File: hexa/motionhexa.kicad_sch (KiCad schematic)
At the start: 1 part, among them J2 Conn_01x13_Socket

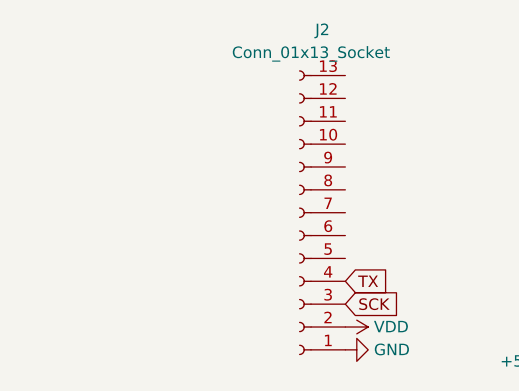
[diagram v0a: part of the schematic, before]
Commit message: checkpoint - hexa design at a size to host two control boards; add board with an rp2040 and a 9dof imu; add a wip for a second board prototype using a BQ25895M to drive higher currents and charge parallel batteries
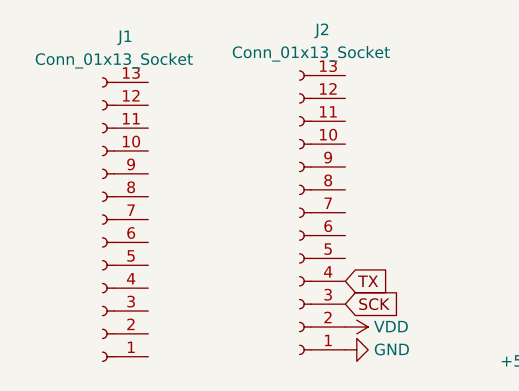
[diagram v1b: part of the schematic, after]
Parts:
- added J1: Conn_01x13_Socket, motionhexa:lipoparallel_pads, symbol Connector:Conn_01x13_Socket
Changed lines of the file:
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@@
+    )
+  )
+  (symbol (lib_id "Connector:Conn_01x13_Socket") (at 89.8652 108.712 180) (unit 1)
+    (in_bom yes) (on_board yes) (dnp no)
+    (property "Reference" "J1" (at 92.4052 88.392 0)
+      (effects (font (size 1.27 1.27)))
+    )
+    (property "Value" "Conn_01x13_Socket" (at 91.1352 90.932 0)
+      (effects (font (size 1.27 1.27)))
+    )
+    (property "Footprint" "motionhexa:lipoparallel_pads" (at 89.8652 108.712 0)
+      (effects (font (size 1.27 1.27)) hide)
+    )
+    (property "Datasheet" "~" (at 89.8652 108.712 0)
+      (effects (font (size 1.27 1.27)) hide)
+    )
+    (property "Designation" "" (at 89.8652 108.712 0)
+      (effects (font (size 1.27 1.27)) hide)
+    )
+    (pin "1")
+    (pin "12")
+    (pin "10")
+    (pin "11")
+    (pin "13")
+    (pin "2")
+    (pin "3")
+    (pin "4")
+    (pin "5")
+    (pin "6")
+    (pin "7")
+    (pin "8")
+    (pin "9")
+    (instances
+      (project "motionhexa"
+        (path "/532d7ce0-7387-4a95-852a-321dca6ae013"
+          (reference "J1") (unit 1)
+        )
+      )
     )
   )

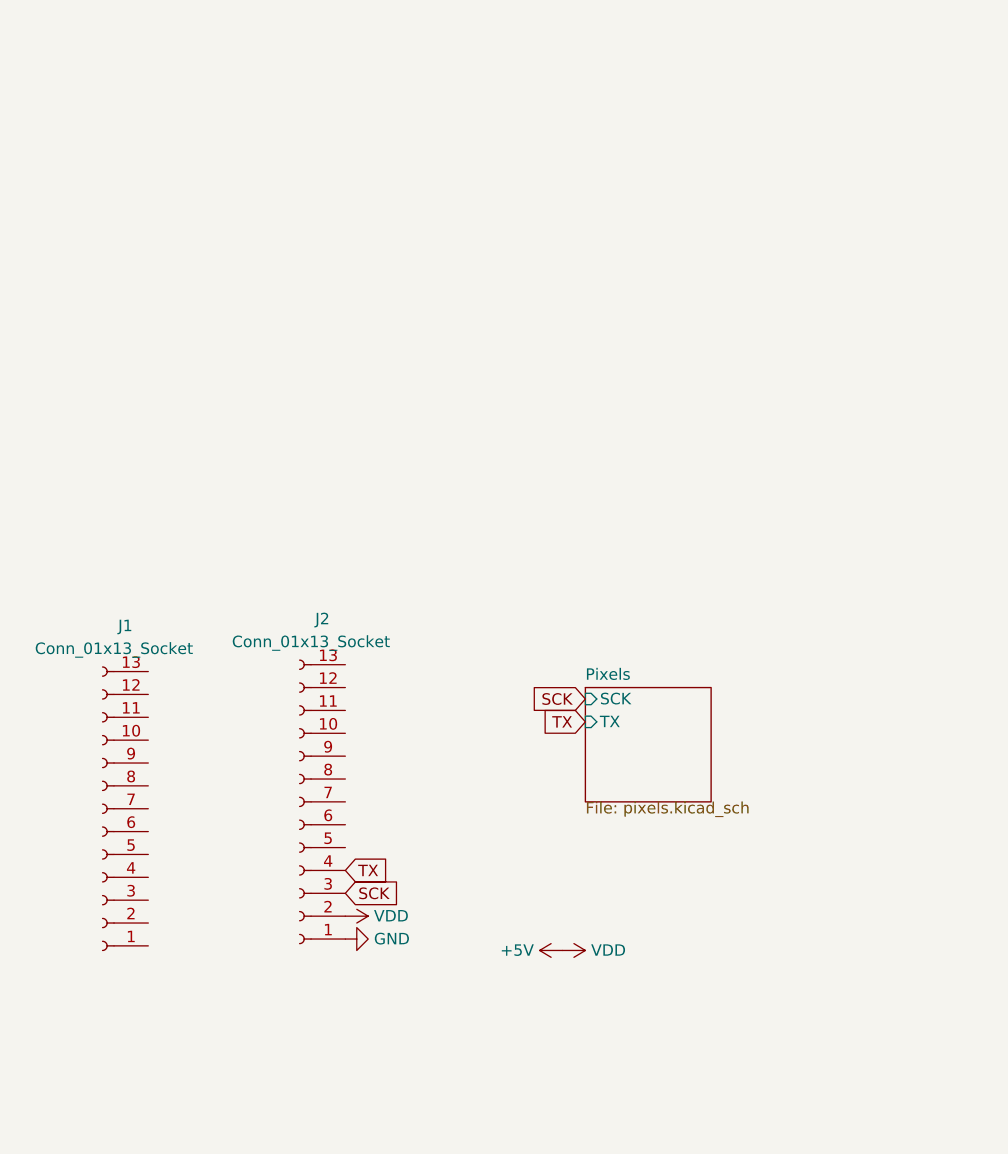
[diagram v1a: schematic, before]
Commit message: layout/zones improvements to rpmotion; pin-matching plan for multiple boards
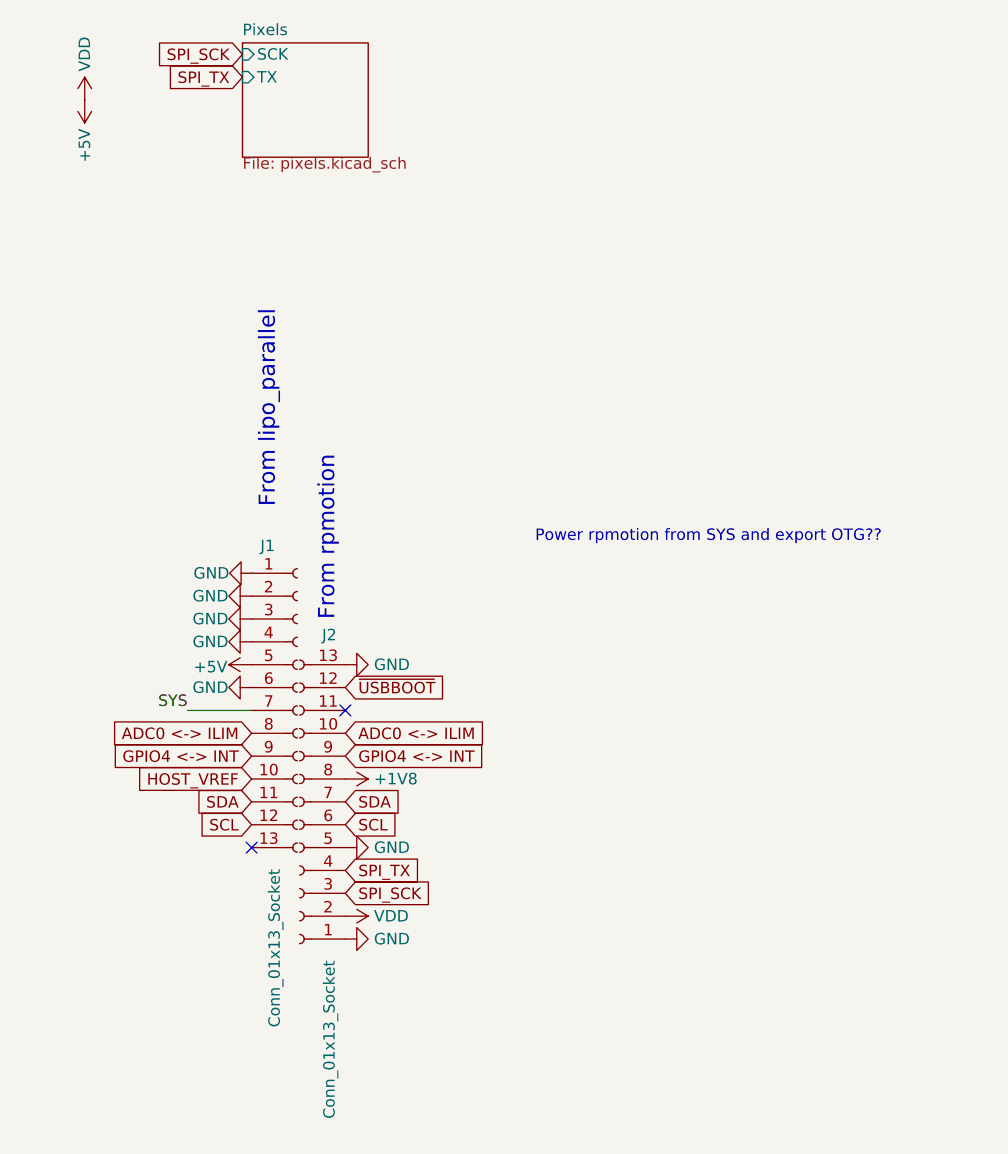
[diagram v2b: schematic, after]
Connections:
- net +5V: now also J1.5 (Pin_5)
- net GND: now also J1.1 (Pin_1), J1.2 (Pin_2), J1.3 (Pin_3), J1.4 (Pin_4), J1.6 (Pin_6), J2.13 (Pin_13), J2.5 (Pin_5)
- net HOST_VREF: now reaches J1.10 (Pin_10)
- net SDA: now reaches J1.11 (Pin_11)
- net SDA: now also J2.7 (Pin_7)
- net SCL: now reaches J1.12 (Pin_12)
- net SCL: now also J2.6 (Pin_6)
- net SYS: now reaches J1.7 (Pin_7)
- net ADC0 <-> ILIM: now reaches J1.8 (Pin_8)
- net ADC0 <-> ILIM: now also J2.10 (Pin_10)
- net GPIO4 <-> INT: now reaches J1.9 (Pin_9)
- net GPIO4 <-> INT: now also J2.9 (Pin_9)
- net ~{USBBOOT}: now reaches J2.12 (Pin_12)
- net +1V8: now reaches J2.8 (Pin_8)
- net SCK renamed SPI_SCK
- net TX renamed SPI_TX
- no-connect marks 0 -> 2
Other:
- note added: "From lipo_parallel"
- note added: "From rpmotion"
- note added: "Power rpmotion from SYS and export OTG??"
- moved on the sheet: J1

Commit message: concept of running rpmotion from SYS line on lipo_parallel so we can still control OTG in software
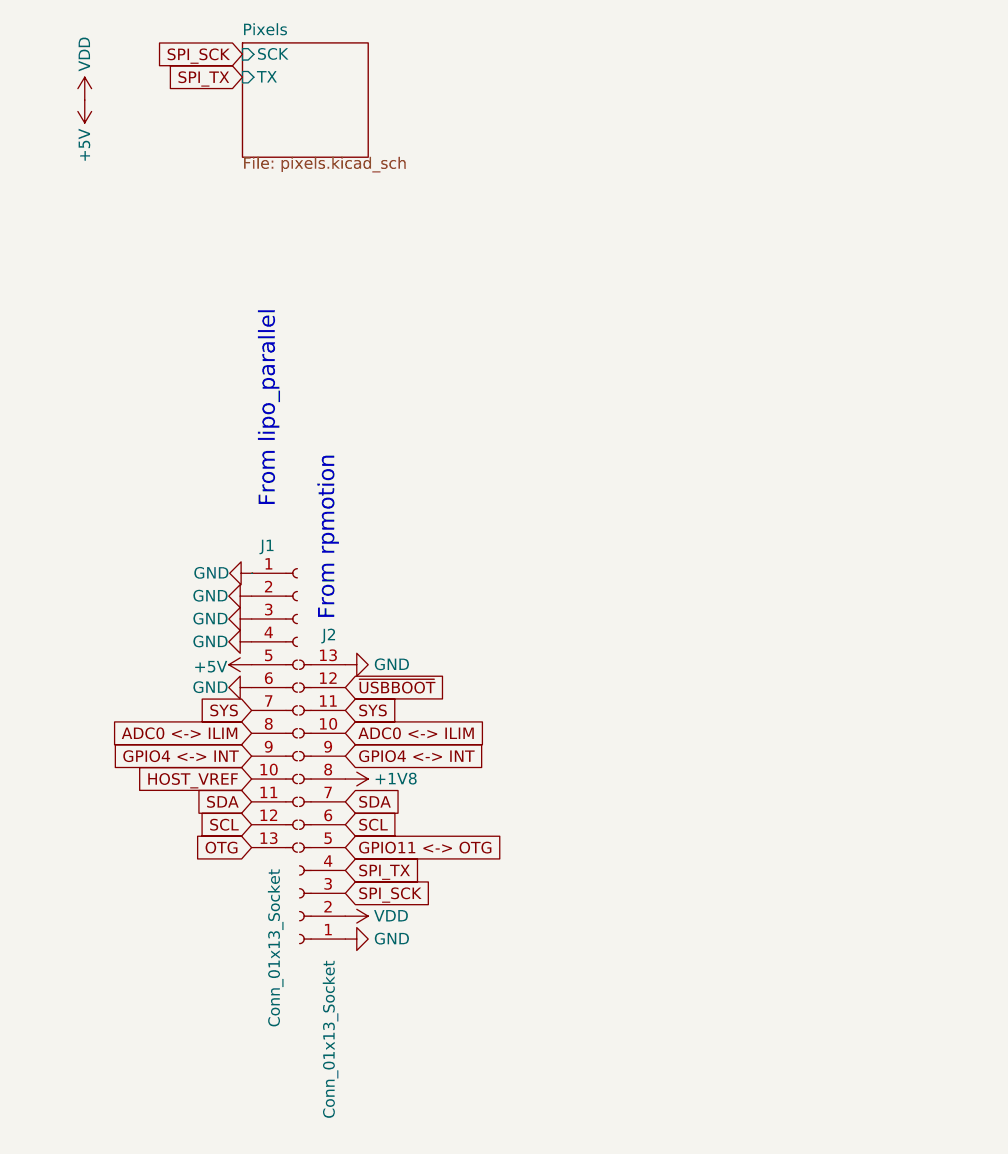
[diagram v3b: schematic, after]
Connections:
- net GND: no longer J2.5 (Pin_5)
- net SYS: now also J2.11 (Pin_11)
- net OTG: now reaches J1.13 (Pin_13)
- new net GPIO11 <-> OTG: J2.5 (Pin_5)
- no-connect marks 2 -> 0
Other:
- note removed: "Power rpmotion from SYS and export OTG??"
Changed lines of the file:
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@@
 (kicad_sch (version 20230121) (generator eeschema)
   (paper "A4")
-  (no_connect (at 116.84 97.79))
-  (no_connect (at 106.426 113.03))
   (wire (pts (xy 106.426 82.55) (xy 106.5276 82.55))
     (stroke (width 0) (type default))
   )
-  (wire (pts (xy 99.314 97.79) (xy 106.426 97.79))
-    (stroke (width 0) (type default))
-  )
   (text "From rpmotion" (at 115.824 87.884 90)
     (effects (font (size 1.8 1.8)) (justify left bottom))
   )
-  (text "Power rpmotion from SYS and export OTG??" (at 137.922 79.248 0)
-    (effects (font (size 1.27 1.27)) (justify left bottom))
-  )
   (text "From lipo_parallel" (at 109.22 53.34 90)
     (effects (font (size 1.8 1.8)) (justify right bottom))
   )
-  (label "SYS" (at 99.314 97.79 180) (fields_autoplaced)
-    (effects (font (size 1.27 1.27)) (justify right bottom))
-  )
   (global_label "ADC0 <-> ILIM" (shape input) (at 106.426 100.33 180) (fields_autoplaced)
     (effects (font (size 1.27 1.27)) (justify right))
@@
     )
   )
+  (global_label "GPIO11 <-> OTG" (shape input) (at 116.84 113.03 0) (fields_autoplaced)
+    (effects (font (size 1.27 1.27)) (justify left))
+    (property "Intersheetrefs" "${INTERSHEET_REFS}" (at 136.94 113.03 0)
+      (effects (font (size 1.27 1.27)) (justify left) hide)
+    )
+  )
   (global_label "SCL" (shape input) (at 116.84 110.49 0) (fields_autoplaced)
     (effects (font (size 1.27 1.27)) (justify left))
@@
     (property "Intersheetrefs" "${INTERSHEET_REFS}" (at 135.0048 100.33 0)
       (effects (font (size 1.27 1.27)) (justify left) hide)
+    )
+  )
+  (global_label "OTG" (shape input) (at 106.426 113.03 180) (fields_autoplaced)
+    (effects (font (size 1.27 1.27)) (justify right))
+    (property "Intersheetrefs" "${INTERSHEET_REFS}" (at 99.8727 113.03 0)
+      (effects (font (size 1.27 1.27)) (justify right) hide)
+    )
+  )
+  (global_label "SYS" (shape input) (at 116.84 97.79 0) (fields_autoplaced)
+    (effects (font (size 1.27 1.27)) (justify left))
+    (property "Intersheetrefs" "${INTERSHEET_REFS}" (at 123.3328 97.79 0)
+      (effects (font (size 1.27 1.27)) (justify left) hide)
+    )
+  )
+  (global_label "SYS" (shape input) (at 106.426 97.79 180) (fields_autoplaced)
+    (effects (font (size 1.27 1.27)) (justify right))
+    (property "Intersheetrefs" "${INTERSHEET_REFS}" (at 99.9332 97.79 0)
+      (effects (font (size 1.27 1.27)) (justify right) hide)
     )
   )
@@
         )
       )
-    )
-  )
-  (symbol (lib_id "power:GND") (at 116.84 113.03 90) (unit 1)
-    (in_bom yes) (on_board yes) (dnp no) (fields_autoplaced)
-    (property "Reference" "#PWR05" (at 123.19 113.03 0)
-      (effects (font (size 1.27 1.27)) hide)
-    )
-    (property "Value" "GND" (at 120.015 113.03 90)
-      (effects (font (size 1.27 1.27)) (justify right))
-    )
-    (property "Footprint" "" (at 116.84 113.03 0)
-      (effects (font (size 1.27 1.27)) hide)
-    )
-    (property "Datasheet" "" (at 116.84 113.03 0)
-      (effects (font (size 1.27 1.27)) hide)
-    )
-    (pin "1")
-    (instances
-      (project "motionhexa"
-        (path "/532d7ce0-7387-4a95-852a-321dca6ae013"
-          (reference "#PWR05") (unit 1)
-        )
-      )

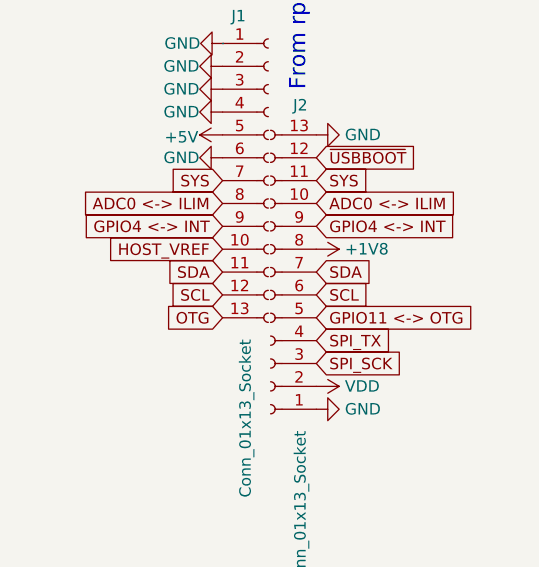
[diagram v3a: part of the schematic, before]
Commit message: flip direction of pixel data flow and redo all the traces; improvements to layout script including using TraceBuilder for gnd and power draws, and a --lock cli option
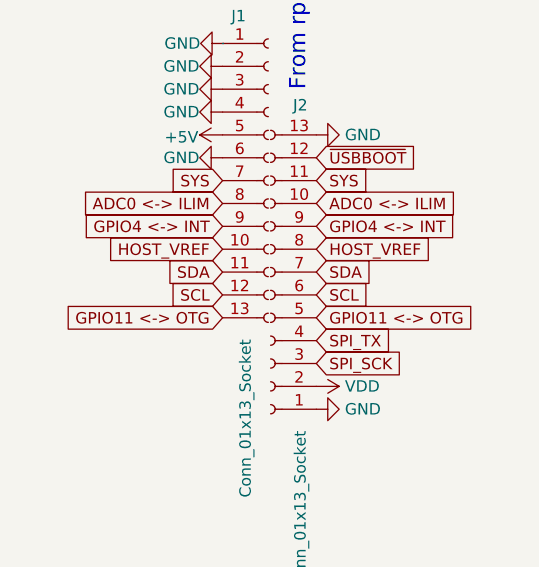
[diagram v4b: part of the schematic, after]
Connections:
- net +1V8 is gone; now on net HOST_VREF: J2.8 (Pin_8)
- net OTG is gone; now on net GPIO11 <-> OTG: J1.13 (Pin_13)
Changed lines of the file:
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@@
+    )
+  )
+  (global_label "HOST_VREF" (shape input) (at 116.84 105.41 0) (fields_autoplaced)
+    (effects (font (size 1.27 1.27)) (justify left))
+    (property "Intersheetrefs" "${INTERSHEET_REFS}" (at 130.2271 105.41 0)
+      (effects (font (size 1.27 1.27)) (justify left) hide)
     )
   )
@@
     (property "Intersheetrefs" "${INTERSHEET_REFS}" (at 135.0653 102.87 0)
       (effects (font (size 1.27 1.27)) (justify left) hide)
+    )
+  )
+  (global_label "GPIO11 <-> OTG" (shape input) (at 106.426 113.03 180) (fields_autoplaced)
+    (effects (font (size 1.27 1.27)) (justify right))
+    (property "Intersheetrefs" "${INTERSHEET_REFS}" (at 86.326 113.03 0)
+      (effects (font (size 1.27 1.27)) (justify right) hide)
     )
   )
@@
     (property "Intersheetrefs" "${INTERSHEET_REFS}" (at 135.0048 100.33 0)
       (effects (font (size 1.27 1.27)) (justify left) hide)
-    )
-  )
-  (global_label "OTG" (shape input) (at 106.426 113.03 180) (fields_autoplaced)
-    (effects (font (size 1.27 1.27)) (justify right))
-    (property "Intersheetrefs" "${INTERSHEET_REFS}" (at 99.8727 113.03 0)
-      (effects (font (size 1.27 1.27)) (justify right) hide)
     )
   )
@@
         )
       )
-    )
-  )
-  (symbol (lib_id "power:+1V8") (at 116.84 105.41 270) (unit 1)
-    (in_bom yes) (on_board yes) (dnp no) (fields_autoplaced)
-    (property "Reference" "#PWR06" (at 113.03 105.41 0)
-      (effects (font (size 1.27 1.27)) hide)
-    )
-    (property "Value" "+1V8" (at 120.015 105.41 90)
-      (effects (font (size 1.27 1.27)) (justify left))
-    )
-    (property "Footprint" "" (at 116.84 105.41 0)
-      (effects (font (size 1.27 1.27)) hide)
-    )
-    (property "Datasheet" "" (at 116.84 105.41 0)
-      (effects (font (size 1.27 1.27)) hide)
-    )
-    (pin "1")
-    (instances
-      (project "motionhexa"
-        (path "/532d7ce0-7387-4a95-852a-321dca6ae013"
-          (reference "#PWR06") (unit 1)
-        )
-      )

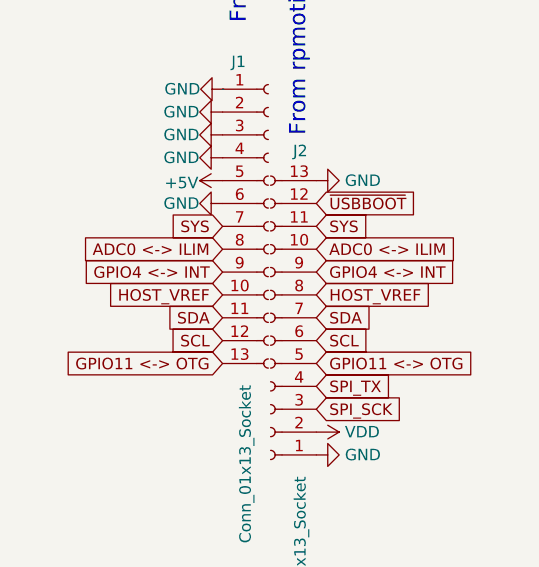
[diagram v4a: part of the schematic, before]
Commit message: make the lipo_parallel pcb taller to fit everything better; lipo_parallel layout concept for battery terminals on the same side - change pin-matchups to work with that better; make motionhexa larger (more pixels) to accomodate that and bc more pixels = better; insert some capacitors with layout script
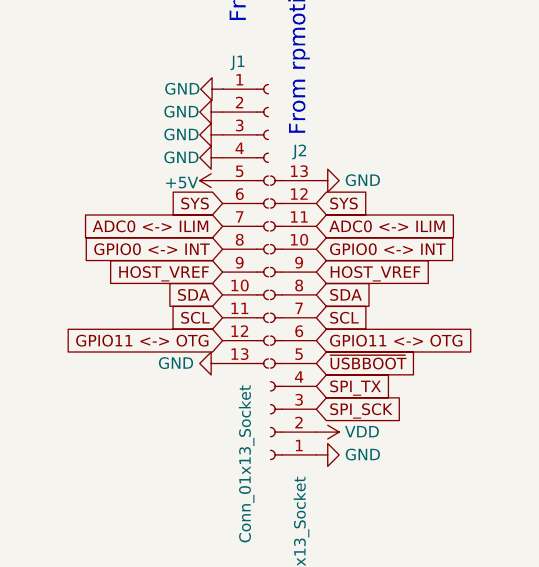
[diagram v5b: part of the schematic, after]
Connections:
- net GPIO4 <-> INT is gone; now on net HOST_VREF: J1.9 (Pin_9), J2.9 (Pin_9)
- net ADC0 <-> ILIM: now also J1.7 (Pin_7), J2.11 (Pin_11); no longer J1.8 (Pin_8), J2.10 (Pin_10)
- net GND: now also J1.13 (Pin_13); no longer J1.6 (Pin_6)
- net GPIO11 <-> OTG: now also J1.12 (Pin_12), J2.6 (Pin_6); no longer J1.13 (Pin_13), J2.5 (Pin_5)
- net HOST_VREF: no longer J1.10 (Pin_10), J2.8 (Pin_8)
- net SCL: now also J1.11 (Pin_11), J2.7 (Pin_7); no longer J1.12 (Pin_12), J2.6 (Pin_6)
- net SDA: now also J1.10 (Pin_10), J2.8 (Pin_8); no longer J1.11 (Pin_11), J2.7 (Pin_7)
- net SYS: now also J1.6 (Pin_6), J2.12 (Pin_12); no longer J1.7 (Pin_7), J2.11 (Pin_11)
- net ~{USBBOOT}: now also J2.5 (Pin_5); no longer J2.12 (Pin_12)
- new net GPIO0 <-> INT: J1.8 (Pin_8), J2.10 (Pin_10)

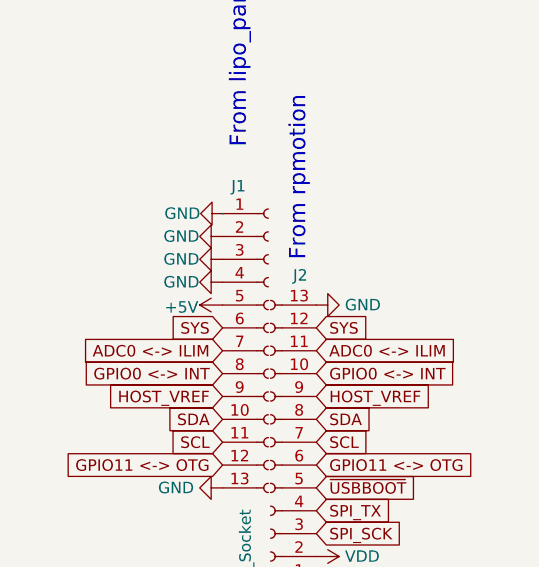
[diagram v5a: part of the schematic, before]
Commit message: first complete wiring
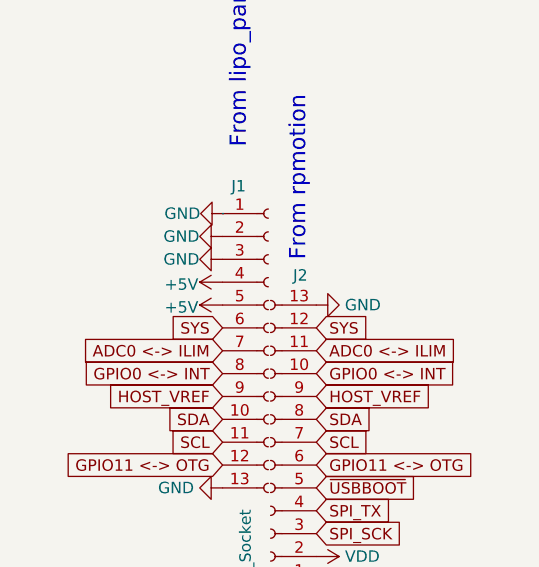
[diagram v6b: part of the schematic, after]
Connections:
- net +5V: now also J1.4 (Pin_4)
- net GND: no longer J1.4 (Pin_4)
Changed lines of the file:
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@@
-    )
-  )
-  (symbol (lib_id "power:GND") (at 106.426 90.17 270) (unit 1)
-    (in_bom yes) (on_board yes) (dnp no)
-    (property "Reference" "#PWR010" (at 100.076 90.17 0)
-      (effects (font (size 1.27 1.27)) hide)
-    )
-    (property "Value" "GND" (at 101.854 90.17 90)
-      (effects (font (size 1.27 1.27)))
-    )
-    (property "Footprint" "" (at 106.426 90.17 0)
-      (effects (font (size 1.27 1.27)) hide)
-    )
-    (property "Datasheet" "" (at 106.426 90.17 0)
-      (effects (font (size 1.27 1.27)) hide)
-    )
-    (pin "1")
-    (instances
-      (project "motionhexa"
-        (path "/532d7ce0-7387-4a95-852a-321dca6ae013"
-          (reference "#PWR010") (unit 1)
-        )
-      )
     )
   )
@@
         )
       )
+    )
+  )
+  (symbol (lib_id "power:+5V") (at 106.426 90.17 90) (unit 1)
+    (in_bom yes) (on_board yes) (dnp no)
+    (property "Reference" "#PWR06" (at 110.236 90.17 0)
+      (effects (font (size 1.27 1.27)) hide)
+    )
+    (property "Value" "+5V" (at 101.854 90.424 90)
+      (effects (font (size 1.27 1.27)))
+    )
+    (property "Footprint" "" (at 106.426 90.17 0)
+      (effects (font (size 1.27 1.27)) hide)
+    )
+    (property "Datasheet" "" (at 106.426 90.17 0)
+      (effects (font (size 1.27 1.27)) hide)
+    )
+    (pin "1")
+    (instances
+      (project "motionhexa"
+        (path "/532d7ce0-7387-4a95-852a-321dca6ae013"
+          (reference "#PWR06") (unit 1)
+        )
+      )
